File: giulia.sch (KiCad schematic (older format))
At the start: 129 parts, among them J1 AVR-ISP-6, SW1 RESET, SW2 BOOT, U1 ATmega32A-PU, Y1 16 MHz

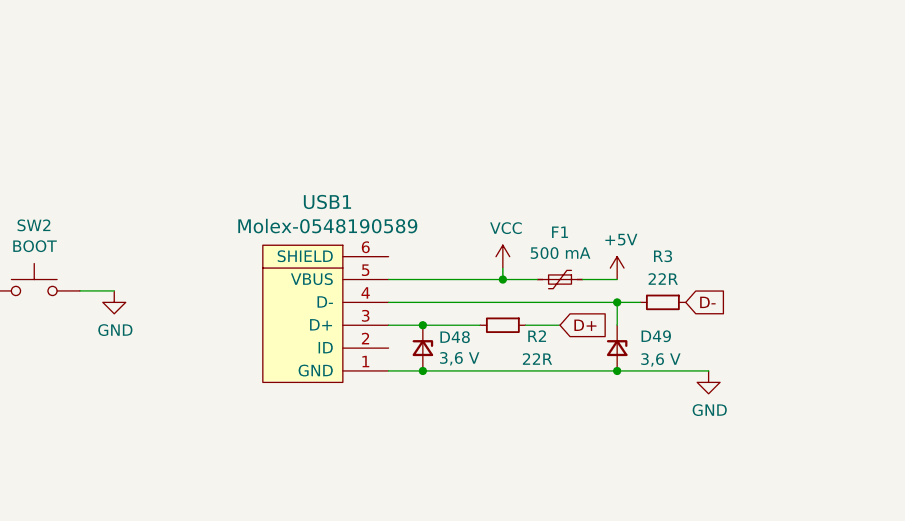
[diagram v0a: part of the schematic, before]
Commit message: added most footprints
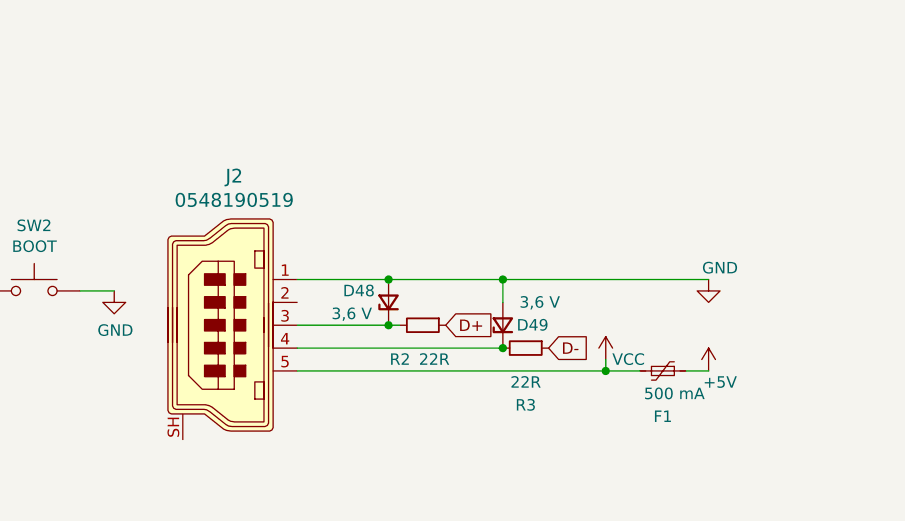
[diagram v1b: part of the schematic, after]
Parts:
- removed USB1: Molex-0548190589, symbol random-keyboard-parts:Molex-0548190589
- added J2: 0548190519, digikey-footprints:USB_Mini_B_Female_548190519, symbol dk_USB-DVI-HDMI-Connectors:0548190519
- C1: footprint (none) -> Capacitor_THT:CP_Radial_D5.0mm_P2.00mm
- C2, C3, C4, C5: footprint (none) -> Capacitor_THT:C_Disc_D3.0mm_W2.0mm_P2.50mm
- D1, D10, D11, D12, D13, D14, D15, D16, D17, D18, D19, D2, D20, D21, D22, D23, D24, D25, D26, D27, D28, D29, D3, D30, D31, D32, D33, D34, D35, D36, D37, D38, D39, D4, D40, D41, D42, D43, D44, D45, D46, D47, D48, D49, D5, D6, D7, D8, D9: footprint (none) -> Diode_THT:D_DO-35_SOD27_P2.54mm_Vertical_KathodeUp
- F1: footprint (none) -> Fuse:Fuse_BelFuse_0ZRE0005FF_L8.3mm_W3.8mm
- J1: footprint (none) -> Connector_PinHeader_2.54mm:PinHeader_2x03_P2.54mm_Horizontal
- R1, R2, R3, R4: footprint (none) -> Resistor_THT:R_Axial_DIN0309_L9.0mm_D3.2mm_P2.54mm_Vertical
- SW1, SW2: footprint (none) -> Button_Switch_THT:SW_PUSH_6mm
- Y1: footprint (none) -> Crystal:Crystal_HC49-U_Horizontal
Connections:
- net GND: now also J2.1
- net VCC: now also J2.5
- net at D48.1 (K), R2.2: now also J2.3
- net at D49.1 (K), R3.2: now also J2.4
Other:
- moved on the sheet: D48, D49, F1, R2, R3

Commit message: all footprints assigned
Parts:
- MX1, MX10, MX11, MX12, MX13, MX14, MX15, MX16, MX17, MX18, MX19, MX21, MX22, MX23, MX25, MX26, MX27, MX28, MX29, MX30, MX32, MX33, MX34, MX35, MX36, MX37, MX38, MX39, MX4, MX40, MX41, MX42, MX43, MX46, MX47, MX5, MX6, MX7, MX8, MX9: footprint (none) -> MX_Alps_Hybrid:MX-1U-NoLED
- MX2, MX20, MX31, MX45: footprint (none) -> MX_Alps_Hybrid:MX-1.25U-NoLED
- MX24: footprint (none) -> MX_Alps_Hybrid:MX-2U-ReversedStabilizers-NoLED
- MX3, MX44: footprint (none) -> MX_Alps_Hybrid:MX-1.5U-NoLED
- OL1: footprint (none) -> Connector_PinHeader_2.54mm:PinHeader_1x04_P2.54mm_Vertical

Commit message: adjusted footprints
changed some footprints based on common parts availability (carbon vs metallic resistors, ceramic condensator pin pitch)
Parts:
- C2, C3, C4, C5: footprint Capacitor_THT:C_Disc_D3.0mm_W2.0mm_P2.50mm -> Capacitor_THT:C_Disc_D5.0mm_W2.5mm_P5.00mm
- R1, R2, R3, R4: footprint Resistor_THT:R_Axial_DIN0309_L9.0mm_D3.2mm_P2.54mm_Vertical -> Resistor_THT:R_Axial_DIN0207_L6.3mm_D2.5mm_P2.54mm_Vertical
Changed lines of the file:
@@
 F 0 "C5" H 1700 4350 50  0000 L CNN
 F 1 "22p" H 1700 4250 50  0000 L CNN
-F 2 "Capacitor_THT:C_Disc_D3.0mm_W2.0mm_P2.50mm" H 1600 4300 50  0001 C CNN
+F 2 "Capacitor_THT:C_Disc_D5.0mm_W2.5mm_P5.00mm" H 1600 4300 50  0001 C CNN
 F 3 "~" H 1600 4300 50  0001 C CNN
 	1    1600 4300
@@
 F 0 "C4" H 1200 4350 50  0000 L CNN
 F 1 "22p" H 1200 4250 50  0000 L CNN
-F 2 "Capacitor_THT:C_Disc_D3.0mm_W2.0mm_P2.50mm" H 1400 4300 50  0001 C CNN
+F 2 "Capacitor_THT:C_Disc_D5.0mm_W2.5mm_P5.00mm" H 1400 4300 50  0001 C CNN
 F 3 "~" H 1400 4300 50  0001 C CNN
 	1    1400 4300
@@
 F 0 "C2" H 1550 6900 50  0000 L CNN
 F 1 "100n" H 1550 6800 50  0000 L CNN
-F 2 "Capacitor_THT:C_Disc_D3.0mm_W2.0mm_P2.50mm" H 1450 6850 50  0001 C CNN
+F 2 "Capacitor_THT:C_Disc_D5.0mm_W2.5mm_P5.00mm" H 1450 6850 50  0001 C CNN
 F 3 "~" H 1450 6850 50  0001 C CNN
 	1    1450 6850
@@
 F 0 "C3" H 1892 6896 50  0000 L CNN
 F 1 "100n" H 1892 6805 50  0000 L CNN
-F 2 "Capacitor_THT:C_Disc_D3.0mm_W2.0mm_P2.50mm" H 1800 6850 50  0001 C CNN
+F 2 "Capacitor_THT:C_Disc_D5.0mm_W2.5mm_P5.00mm" H 1800 6850 50  0001 C CNN
 F 3 "~" H 1800 6850 50  0001 C CNN
 	1    1800 6850
@@
 F 0 "R1" H 2009 3196 50  0000 L CNN
 F 1 "10k" H 2009 3105 50  0000 L CNN
-F 2 "Resistor_THT:R_Axial_DIN0309_L9.0mm_D3.2mm_P2.54mm_Vertical" H 1950 3150 50  0001 C CNN
+F 2 "Resistor_THT:R_Axial_DIN0207_L6.3mm_D2.5mm_P2.54mm_Vertical" H 1950 3150 50  0001 C CNN
 F 3 "~" H 1950 3150 50  0001 C CNN
 	1    1950 3150
@@
 F 0 "R2" V 5650 6850 50  0000 C CNN
 F 1 "22R" V 5650 7000 50  0000 C CNN
-F 2 "Resistor_THT:R_Axial_DIN0309_L9.0mm_D3.2mm_P2.54mm_Vertical" H 5500 6950 50  0001 C CNN
+F 2 "Resistor_THT:R_Axial_DIN0207_L6.3mm_D2.5mm_P2.54mm_Vertical" H 5500 6950 50  0001 C CNN
 F 3 "~" H 5500 6950 50  0001 C CNN
 	1    5500 6950
@@
 F 0 "R3" V 6200 7050 50  0000 C CNN
 F 1 "22R" V 6100 7050 50  0000 C CNN
-F 2 "Resistor_THT:R_Axial_DIN0309_L9.0mm_D3.2mm_P2.54mm_Vertical" H 5950 7050 50  0001 C CNN
+F 2 "Resistor_THT:R_Axial_DIN0207_L6.3mm_D2.5mm_P2.54mm_Vertical" H 5950 7050 50  0001 C CNN
 F 3 "~" H 5950 7050 50  0001 C CNN
 	1    5950 7050
@@
 F 0 "R4" V 3754 4500 50  0000 C CNN
 F 1 "470R" V 3845 4500 50  0000 C CNN
-F 2 "Resistor_THT:R_Axial_DIN0309_L9.0mm_D3.2mm_P2.54mm_Vertical" H 3950 4500 50  0001 C CNN
+F 2 "Resistor_THT:R_Axial_DIN0207_L6.3mm_D2.5mm_P2.54mm_Vertical" H 3950 4500 50  0001 C CNN
 F 3 "~" H 3950 4500 50  0001 C CNN
 	1    3950 4500

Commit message: Started work on PCB footprints
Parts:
- D1, D10, D11, D12, D13, D14, D15, D16, D17, D18, D19, D2, D20, D21, D22, D23, D24, D25, D26, D27, D28, D29, D3, D30, D31, D32, D33, D34, D35, D36, D37, D38, D39, D4, D40, D41, D42, D43, D44, D45, D46, D47, D48, D49, D5, D6, D7, D8, D9: footprint Diode_THT:D_DO-35_SOD27_P2.54mm_Vertical_KathodeUp -> Diode_THT:D_DO-35_SOD27_P7.62mm_Horizontal
- J1: footprint Connector_PinHeader_2.54mm:PinHeader_2x03_P2.54mm_Horizontal -> Connector_PinHeader_2.54mm:PinHeader_2x03_P2.54mm_Vertical
- R1, R2, R3, R4: footprint Resistor_THT:R_Axial_DIN0207_L6.3mm_D2.5mm_P2.54mm_Vertical -> Resistor_THT:R_Axial_DIN0207_L6.3mm_D2.5mm_P10.16mm_Horizontal
- Y1: footprint Crystal:Crystal_HC49-U_Horizontal -> Crystal:Crystal_HC49-U_Vertical
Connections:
- net COL0: now also U1.24 (PC2); no longer U1.40 (PA0)
- net COL1: now also U1.25 (PC3); no longer U1.39 (PA1)
- net COL10: now also U1.39 (PA1); no longer U1.25 (PC3)
- net COL11: now also U1.40 (PA0); no longer U1.24 (PC2)
- net COL2: now also U1.26 (PC4); no longer U1.38 (PA2)
- net COL3: now also U1.27 (PC5); no longer U1.37 (PA3)
- net COL4: now also U1.33 (PA7); no longer U1.36 (PA4)
- net COL5: now also U1.34 (PA6); no longer U1.35 (PA5)
- net COL6: now also U1.35 (PA5); no longer U1.34 (PA6)
- net COL7: now also U1.36 (PA4); no longer U1.33 (PA7)
- net COL8: now also U1.37 (PA3); no longer U1.27 (PC5)
- net COL9: now also U1.38 (PA2); no longer U1.26 (PC4)

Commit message: Adjusting physical component layout
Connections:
- net at U1.18 (PD4): no longer SW2.1
- net BOOT: now reaches U1.5 (PB4)
- net BOOT: now also SW2.1
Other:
- moved on the sheet: SW2
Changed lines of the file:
@@
 L Switch:SW_Push SW2
 U 1 1 6110F719
-P 3800 6800
-F 0 "SW2" H 3800 7085 50  0000 C CNN
-F 1 "BOOT" H 3800 6994 50  0000 C CNN
-F 2 "Button_Switch_THT:SW_PUSH_6mm" H 3800 7000 50  0001 C CNN
-F 3 "~" H 3800 7000 50  0001 C CNN
-	1    3800 6800
+P 4850 5850
+F 0 "SW2" H 4850 6135 50  0000 C CNN
+F 1 "BOOT" H 4850 6044 50  0000 C CNN
+F 2 "Button_Switch_THT:SW_PUSH_6mm" H 4850 6050 50  0001 C CNN
+F 3 "~" H 4850 6050 50  0001 C CNN
+	1    4850 5850
 	1    0    0    -1
 $EndComp
 Wire Wire Line
-	3600 6800 3250 6800
+	4650 5850 4300 5850
 $Comp
 L power:GND #PWR010
 U 1 1 611102A9
-P 4150 6800
-F 0 "#PWR010" H 4150 6550 50  0001 C CNN
-F 1 "GND" H 4155 6627 50  0000 C CNN
-F 2 "" H 4150 6800 50  0001 C CNN
-F 3 "" H 4150 6800 50  0001 C CNN
-	1    4150 6800
+P 5200 5850
+F 0 "#PWR010" H 5200 5600 50  0001 C CNN
+F 1 "GND" H 5205 5677 50  0000 C CNN
+F 2 "" H 5200 5850 50  0001 C CNN
+F 3 "" H 5200 5850 50  0001 C CNN
+	1    5200 5850
 	1    0    0    -1
 $EndComp
 Wire Wire Line
-	4150 6800 4000 6800
+	5200 5850 5050 5850
 $Comp
 L dk_USB-DVI-HDMI-Connectors:0548190519 J2
@@
 Wire Wire Line
 	5350 6750 4950 6750
+Text GLabel 3250 5000 2    50   Input ~ 0
+BOOT
+Text GLabel 4300 5850 0    50   Input ~ 0
+BOOT
 $EndSCHEMATC

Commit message: PCB progress
finally placed RGB footprints, added own footprint lib for easy silkscreen adjustment etc.
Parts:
- D1, D10, D11, D12, D13, D14, D15, D16, D17, D18, D19, D2, D20, D21, D22, D23, D24, D25, D26, D27, D28, D29, D3, D30, D31, D32, D33, D34, D35, D36, D37, D38, D39, D4, D40, D41, D42, D43, D44, D45, D46, D47, D5, D6, D7, D8, D9: footprint Diode_THT:D_DO-35_SOD27_P7.62mm_Horizontal -> giulia:D_DO-35_SOD27_P7.62mm_Horizontal_Giulia

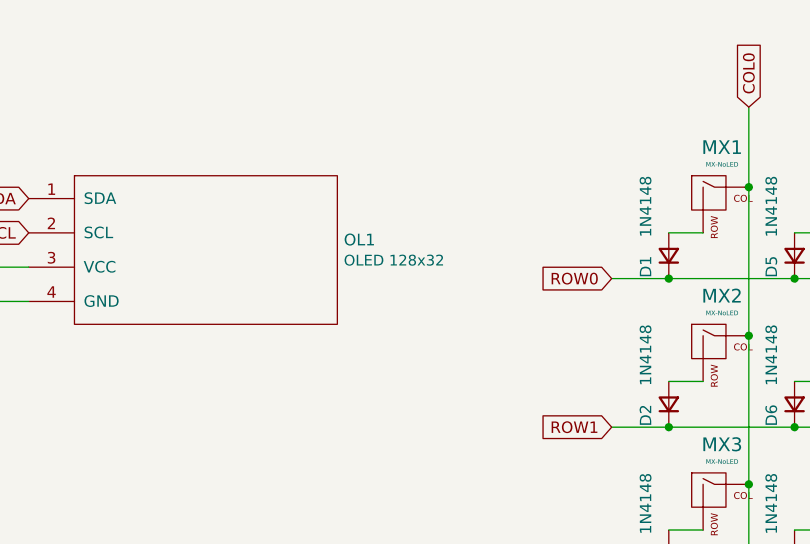
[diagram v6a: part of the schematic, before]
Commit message: cleaned up libs, removed submodules
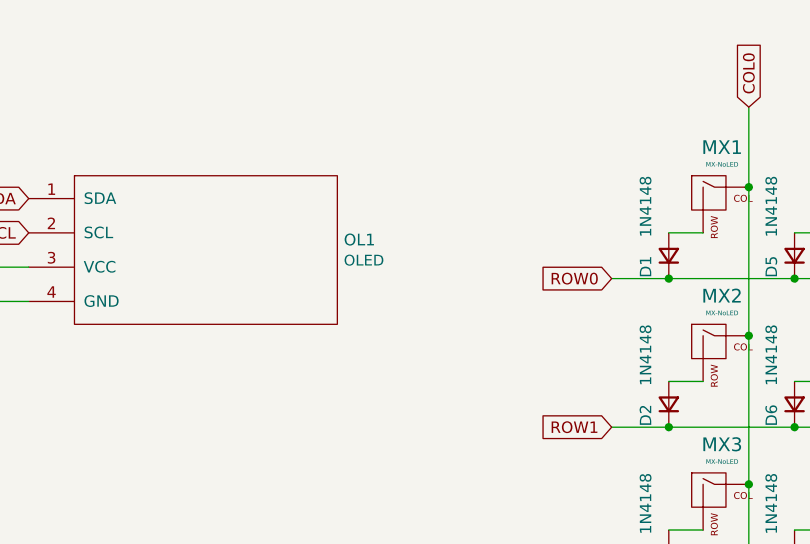
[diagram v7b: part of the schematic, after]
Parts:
- removed OL1: OLED 128x32, Connector_PinHeader_2.54mm:PinHeader_1x04_P2.54mm_Vertical, symbol kbd:OLED
- added OL1: OLED, giulia:OLED, symbol giulia:OLED
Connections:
- net +5V: now also OL1.3 (VCC)
- net GND: now also OL1.4 (GND)
- net SCL: now also OL1.2 (SCL)
- net SDA: now also OL1.1 (SDA)
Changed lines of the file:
@@
 Text GLabel 3250 5600 2    50   Input ~ 0
 SDA
-$Comp
-L kbd:OLED OL1
-U 1 1 615D634B
-P 2550 1550
-F 0 "OL1" H 3178 1619 51  0000 L CNN
-F 1 "OLED 128x32" H 3178 1529 47  0000 L CNN
-F 2 "Connector_PinHeader_2.54mm:PinHeader_1x04_P2.54mm_Vertical" H 2550 1650 60  0001 C CNN
-F 3 "" H 2550 1650 60  0001 C CNN
-	1    2550 1550
-	1    0    0    -1
-$EndComp
 Text GLabel 1800 1450 0    50   Input ~ 0
 SCL
@@
 Text GLabel 4300 5850 0    50   Input ~ 0
 BOOT
+$Comp
+L giulia:OLED OL1
+U 1 1 612B1F40
+P 2550 1550
+F 0 "OL1" H 3178 1619 51  0000 L CNN
+F 1 "OLED" H 3178 1529 47  0000 L CNN
+F 2 "giulia:OLED" H 2550 1650 60  0001 C CNN
+F 3 "" H 2550 1650 60  0001 C CNN
+	1    2550 1550
+	1    0    0    -1
+$EndComp
 $EndSCHEMATC

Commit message: rev1 of routing done
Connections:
- net RGB: now also U1.18 (PD4); no longer U1.20 (PD6)
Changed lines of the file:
@@
 Text GLabel 3250 3700 2    50   Input ~ 0
 COL11
-Text GLabel 3250 7000 2    50   Input ~ 0
+Text GLabel 3250 6800 2    50   Input ~ 0
 RGB
 Text GLabel 3250 5500 2    50   Input ~ 0
